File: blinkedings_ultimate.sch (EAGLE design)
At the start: 34 parts, among them IC1 FT232RL, T1 BC807-40, T4 BC847, T5 BC847, T6 BC847

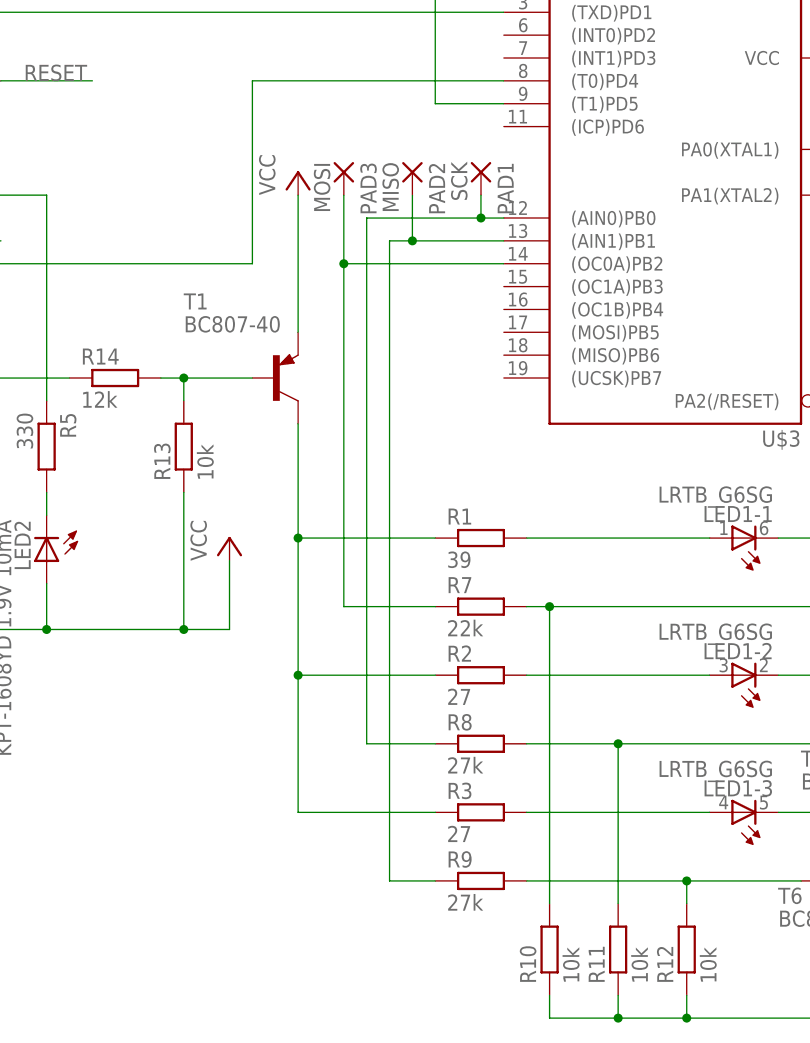
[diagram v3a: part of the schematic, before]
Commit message: fix wrong sck/miso/mosi pins
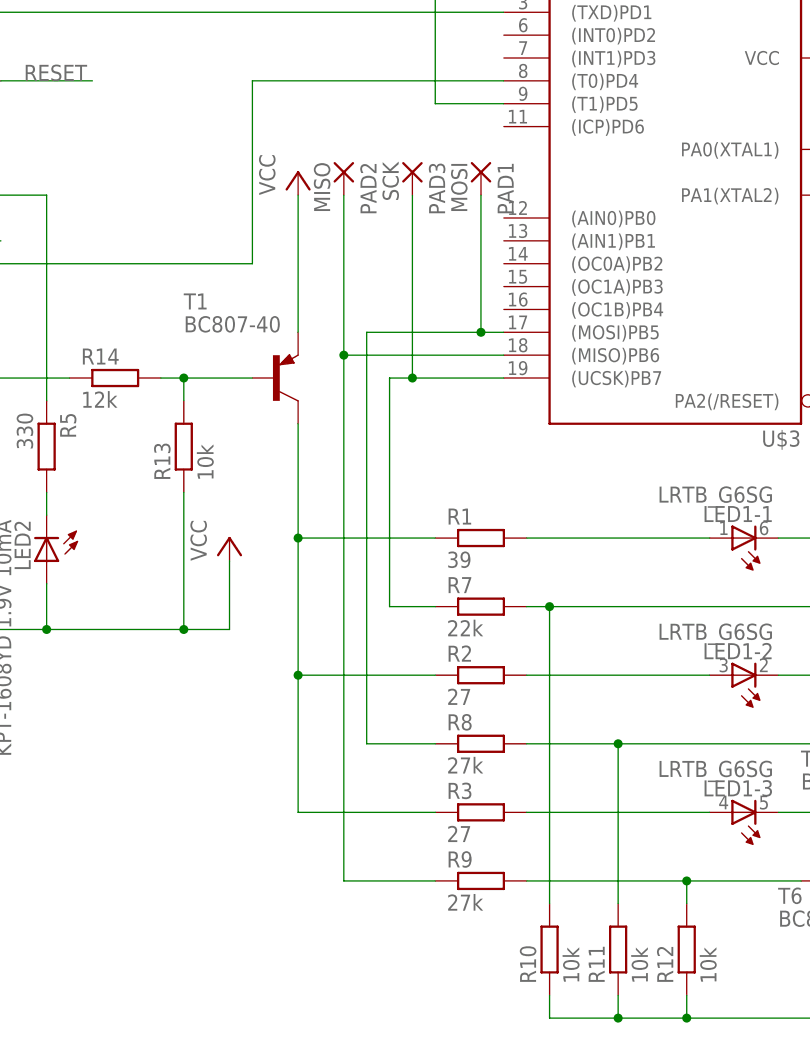
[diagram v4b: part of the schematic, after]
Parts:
- PAD1: value SCK -> MOSI
- PAD3: value MOSI -> SCK
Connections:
- removed net N$14: PAD2.P, R9.1, U$3.(AIN1)PB1
- new net N$22: PAD1.P, R8.1, U$3.(MOSI)PB5
- net N$15: now also PAD2.P, R9.1, U$3.(MISO)PB6; no longer PAD1.P, R8.1, U$3.(AIN0)PB0
- net N$16: now also U$3.(UCSK)PB7; no longer U$3.(OC0A)PB2
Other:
- moved on the sheet: PAD2, PAD3
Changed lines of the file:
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@@
 <part name="C3" library="resistor" deviceset="CPOL-EU" device="SMCC" value="4.7uF"/>
 <part name="U$2" library="usb" deviceset="USB-PLUG" device="-A-SMD"/>
-<part name="PAD1" library="wirepad" deviceset="SMD2" device="" value="SCK"/>
+<part name="PAD1" library="wirepad" deviceset="SMD2" device="" value="MOSI"/>
 <part name="PAD2" library="wirepad" deviceset="SMD2" device="" value="MISO"/>
-<part name="PAD3" library="wirepad" deviceset="SMD2" device="" value="MOSI"/>
+<part name="PAD3" library="wirepad" deviceset="SMD2" device="" value="SCK"/>
 <part name="PAD4" library="wirepad" deviceset="SMD2" device="" value="RESET"/>
 <part name="R4" library="resistor" deviceset="R-EU_" device="R0603" value="10k"/>
@@
 <instance part="U$2" gate="G$1" x="25.4" y="33.02"/>
 <instance part="PAD1" gate="1" x="152.4" y="40.64" rot="R270"/>
-<instance part="PAD2" gate="1" x="144.78" y="40.64" rot="R270"/>
-<instance part="PAD3" gate="1" x="137.16" y="40.64" rot="R270"/>
+<instance part="PAD2" gate="1" x="137.16" y="40.64" rot="R270"/>
+<instance part="PAD3" gate="1" x="144.78" y="40.64" rot="R270"/>
 <instance part="PAD4" gate="1" x="208.28" y="25.4" rot="R270"/>
 <instance part="R4" gate="G$1" x="215.9" y="15.24"/>
@@
 </segment>
 </net>
-<net name="N$14" class="0">
-<segment>
-<wire x1="142.24" y1="-38.1" x2="142.24" y2="33.02" width="0.1524" layer="91"/>
-<pinref part="U$3" gate="G$1" pin="(AIN1)PB1"/>
-<wire x1="142.24" y1="33.02" x2="144.78" y2="33.02" width="0.1524" layer="91"/>
-<pinref part="PAD2" gate="1" pin="P"/>
-<wire x1="144.78" y1="33.02" x2="154.94" y2="33.02" width="0.1524" layer="91"/>
-<wire x1="144.78" y1="38.1" x2="144.78" y2="33.02" width="0.1524" layer="91"/>
-<junction x="144.78" y="33.02"/>
-<pinref part="R9" gate="G$1" pin="1"/>
-<wire x1="142.24" y1="-38.1" x2="147.32" y2="-38.1" width="0.1524" layer="91"/>
-</segment>
-</net>
-<net name="N$15" class="0">
-<segment>
-<wire x1="139.7" y1="35.56" x2="139.7" y2="-22.86" width="0.1524" layer="91"/>
-<pinref part="U$3" gate="G$1" pin="(AIN0)PB0"/>
-<wire x1="139.7" y1="35.56" x2="152.4" y2="35.56" width="0.1524" layer="91"/>
-<pinref part="PAD1" gate="1" pin="P"/>
-<wire x1="152.4" y1="35.56" x2="154.94" y2="35.56" width="0.1524" layer="91"/>
-<wire x1="152.4" y1="38.1" x2="152.4" y2="35.56" width="0.1524" layer="91"/>
-<junction x="152.4" y="35.56"/>
-<pinref part="R8" gate="G$1" pin="1"/>
-<wire x1="139.7" y1="-22.86" x2="147.32" y2="-22.86" width="0.1524" layer="91"/>
-</segment>
-</net>
 <net name="N$16" class="0">
 <segment>
-<wire x1="137.16" y1="30.48" x2="137.16" y2="-7.62" width="0.1524" layer="91"/>
-<pinref part="U$3" gate="G$1" pin="(OC0A)PB2"/>
-<wire x1="137.16" y1="30.48" x2="154.94" y2="30.48" width="0.1524" layer="91"/>
+<pinref part="R7" gate="G$1" pin="1"/>
+<wire x1="142.24" y1="17.78" x2="142.24" y2="-7.62" width="0.1524" layer="91"/>
+<wire x1="147.32" y1="-7.62" x2="142.24" y2="-7.62" width="0.1524" layer="91"/>
+<pinref part="U$3" gate="G$1" pin="(UCSK)PB7"/>
+<wire x1="142.24" y1="17.78" x2="144.78" y2="17.78" width="0.1524" layer="91"/>
 <pinref part="PAD3" gate="1" pin="P"/>
-<wire x1="137.16" y1="38.1" x2="137.16" y2="30.48" width="0.1524" layer="91"/>
-<junction x="137.16" y="30.48"/>
-<pinref part="R7" gate="G$1" pin="1"/>
-<wire x1="147.32" y1="-7.62" x2="137.16" y2="-7.62" width="0.1524" layer="91"/>
+<wire x1="144.78" y1="17.78" x2="154.94" y2="17.78" width="0.1524" layer="91"/>
+<wire x1="144.78" y1="38.1" x2="144.78" y2="17.78" width="0.1524" layer="91"/>
+<junction x="144.78" y="17.78"/>
 </segment>
 </net>
@@
 </segment>
 </net>
+<net name="N$22" class="0">
+<segment>
+<pinref part="R8" gate="G$1" pin="1"/>
+<wire x1="139.7" y1="22.86" x2="139.7" y2="-22.86" width="0.1524" layer="91"/>
+<wire x1="139.7" y1="-22.86" x2="147.32" y2="-22.86" width="0.1524" layer="91"/>
+<pinref part="U$3" gate="G$1" pin="(MOSI)PB5"/>
+<wire x1="139.7" y1="22.86" x2="152.4" y2="22.86" width="0.1524" layer="91"/>
+<pinref part="PAD1" gate="1" pin="P"/>
+<wire x1="152.4" y1="22.86" x2="154.94" y2="22.86" width="0.1524" layer="91"/>
+<wire x1="152.4" y1="38.1" x2="152.4" y2="22.86" width="0.1524" layer="91"/>
+<junction x="152.4" y="22.86"/>
+</segment>
+</net>
+<net name="N$15" class="0">
+<segment>
+<wire x1="137.16" y1="-38.1" x2="137.16" y2="20.32" width="0.1524" layer="91"/>
+<pinref part="R9" gate="G$1" pin="1"/>
+<wire x1="137.16" y1="-38.1" x2="147.32" y2="-38.1" width="0.1524" layer="91"/>
+<pinref part="U$3" gate="G$1" pin="(MISO)PB6"/>
+<wire x1="154.94" y1="20.32" x2="137.16" y2="20.32" width="0.1524" layer="91"/>
+<pinref part="PAD2" gate="1" pin="P"/>
+<wire x1="137.16" y1="38.1" x2="137.16" y2="20.32" width="0.1524" layer="91"/>
+<junction x="137.16" y="20.32"/>
+</segment>
+</net>
